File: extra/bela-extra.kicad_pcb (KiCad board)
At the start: 2 copper layers, 63 x 85.3 mm, 62 parts, among them P1 bbbp9, P10 GU128x64E-U100, P11 gu140x16j-7002, P12 digital_in, P13 digital_out, P14 ext_power, P2 bbbp8, P3 enc+btn1, P4 enc+btn2, P5 power_in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

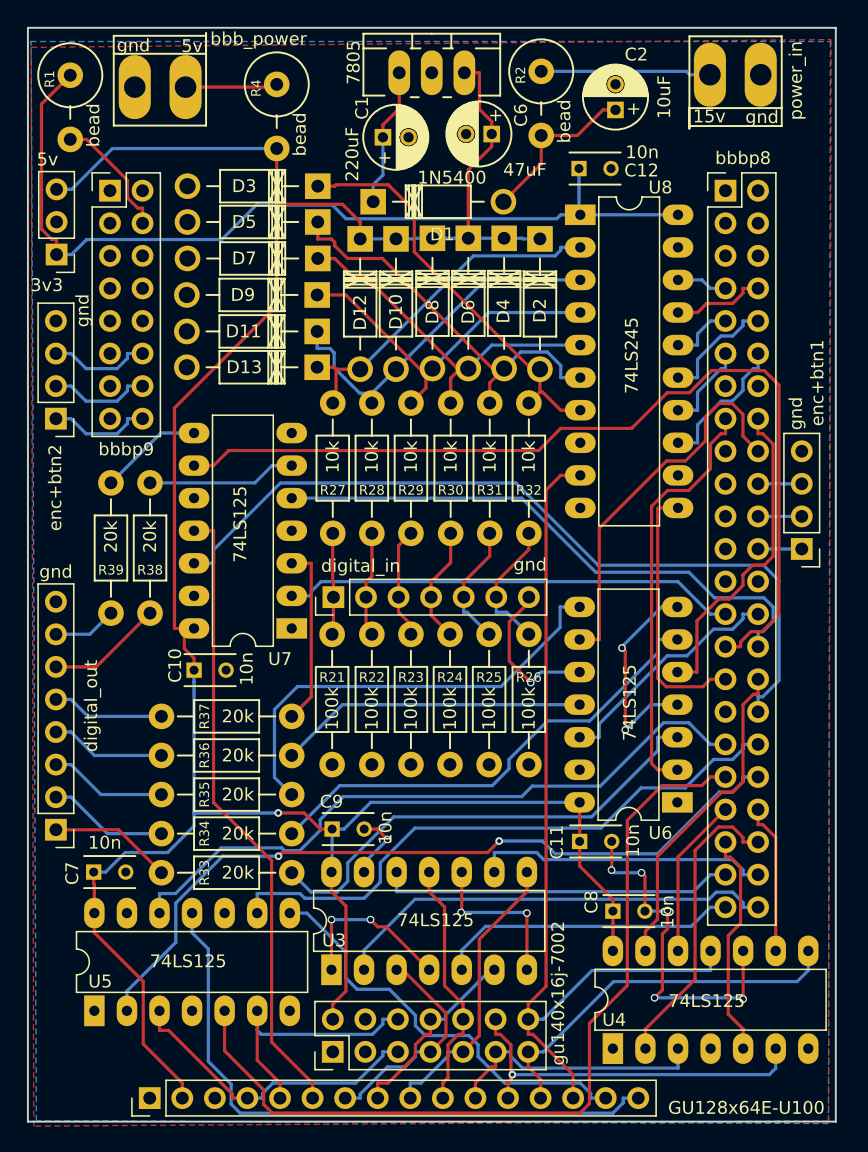
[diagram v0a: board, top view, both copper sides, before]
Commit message: ditched power, remapped a bunch of io
should have all the emmc and lcd lines disabled at boot
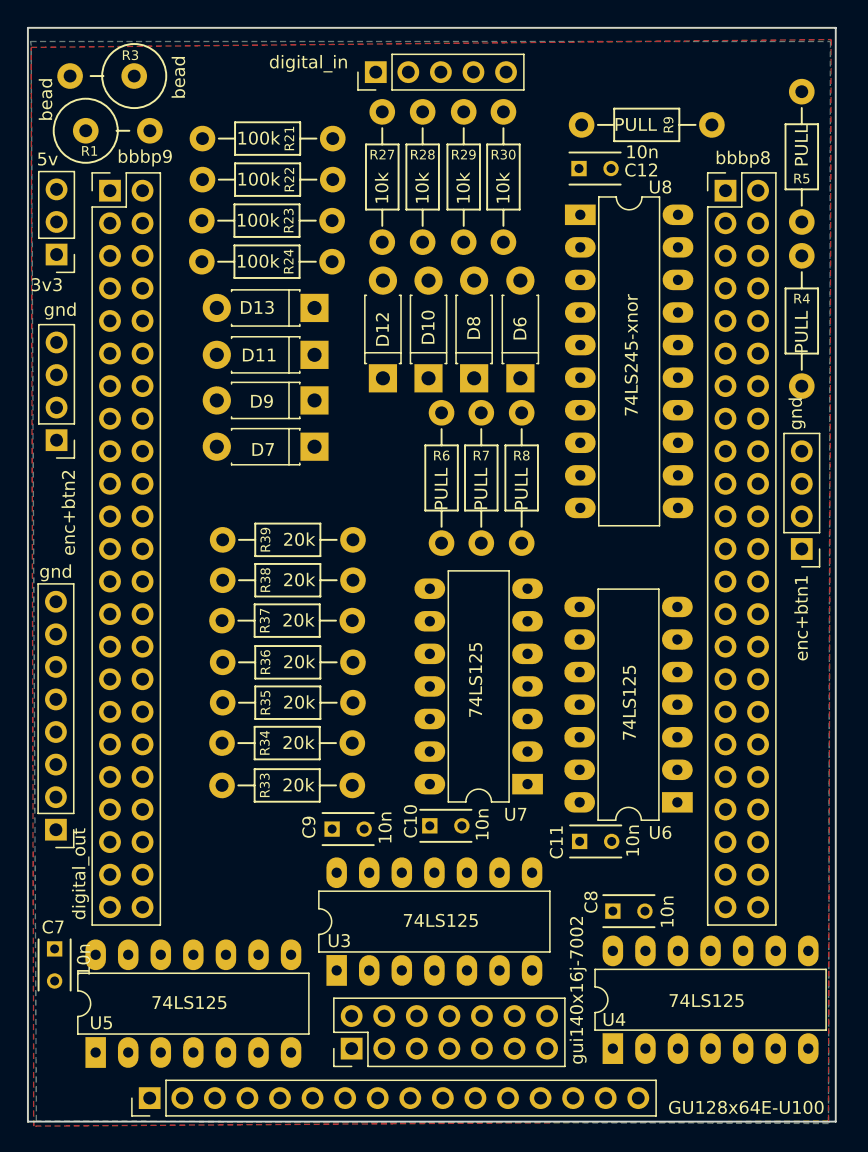
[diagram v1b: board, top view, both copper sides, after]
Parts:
- removed C1: 220uF, Capacitors_ThroughHole:C_Radial_D5_L11_P2
- removed C2: 10uF, Capacitors_ThroughHole:C_Radial_D5_L11_P2
- removed C6: 47uF, Capacitors_ThroughHole:C_Radial_D5_L11_P2
- removed D1: 1N5400, Diodes_ThroughHole:Diode_DO-41_SOD81_Horizontal_RM10
- removed D2, D3, D4, D5: D, Diodes_ThroughHole:Diode_DO-41_SOD81_Horizontal_RM10
- removed P5: power_in, mta-156:MTA-156-2
- removed P6: bbb_power, mta-156:MTA-156-2
- removed R2: bead, xnorman:Resistor_Vertical_RM5mm-xnor
- removed R25, R26: 100k, xnorman:Resistor_Horizontal_RM10mm-xnorman
- removed R31, R32: 10k, xnorman:Resistor_Horizontal_RM10mm-xnorman
- removed U2: 7805, TO_SOT_Packages_THT:TO-220_Neutral123_Vertical_LargePads
- added R3: bead, xnorman:Resistor_Vertical_RM5mm-xnor, F.Cu at (24.8, 16.5)
- added R5: PULL, xnorman:Resistor_Horizontal_RM10mm-xnorman, F.Cu at (79.3, 17.7)
- added R6: PULL, xnorman:Resistor_Horizontal_RM10mm-xnorman, F.Cu at (51.3, 52.9)
- added R7: PULL, xnorman:Resistor_Horizontal_RM10mm-xnorman, F.Cu at (54.4, 52.9)
- added R8: PULL, xnorman:Resistor_Horizontal_RM10mm-xnorman, F.Cu at (57.5, 52.9)
- added R9: PULL, xnorman:Resistor_Horizontal_RM10mm-xnorman, F.Cu at (62.2, 20.3)
- D10, D11, D12, D13, D6, D7, D8, D9: footprint Diodes_ThroughHole:Diode_DO-41_SOD81_Horizontal_RM10 -> Diodes_ThroughHole:D_DO-41_SOD81_P7.62mm_Horizontal
- P1: footprint Pin_Headers:Pin_Header_Straight_2x08_Pitch2.54mm -> Pin_Headers:Pin_Header_Straight_2x23_Pitch2.54mm
- P11: value gu140x16j-7002 -> gui140x16j-7002
- P12: footprint Pin_Headers:Pin_Header_Straight_1x07_Pitch2.54mm -> Pin_Headers:Pin_Header_Straight_1x05_Pitch2.54mm
- R4: value bead -> PULL; footprint xnorman:Resistor_Vertical_RM5mm-xnor -> xnorman:Resistor_Horizontal_RM10mm-xnorman
- U8: value 74LS245 -> 74LS245-xnor
- moved R21 49.9 mm to (32.6, 21.3), turned to 0 degrees
- moved R22 47.5 mm to (32.6, 24.5), turned to 0 degrees
- moved R4 46.0 mm to (79.3, 40.6), turned to 90 degrees
- moved R23 45.4 mm to (32.6, 27.7), turned to 0 degrees
- moved R24 43.7 mm to (32.6, 30.9), turned to 0 degrees
- moved P12 41.1 mm to (46.1, 16.2)
- moved C10 22.0 mm to (50.3, 74.9)
- moved U7 22.0 mm to (58.0, 71.7)
- moved R39 19.4 mm to (44.3, 52.6), turned to 180 degrees
- moved R38 17.6 mm to (44.3, 55.8), turned to 180 degrees
- moved D7 14.7 mm to (41.4, 45.4)
- moved R29 13.2 mm to (53.0, 29.4), turned to 90 degrees
- moved R30 13.2 mm to (56.1, 29.4), turned to 90 degrees
- moved R28 13.2 mm to (49.8, 29.4), turned to 90 degrees
- moved R27 13.1 mm to (46.6, 29.4), turned to 90 degrees
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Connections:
- P1 pad 1: (no net) -> GND
- P1 pad 2: (no net) -> GND
- P1 pad 5: (no net) -> Net-(P1-Pad5)
- P12 pad 5: Net-(P12-Pad5) -> GND
- P2 pad 11: beladigin5 -> bb-digitalInEnable
- P2 pad 12: beladigin6 -> bb-vfdCTRLenable
- P2 pad 13: (no net) -> bb-encin1-btn
- P2 pad 14: (no net) -> bb-vfdDOUTenable
- P2 pad 20: encin1-btn -> (no net)
- P2 pad 22: encin1-b -> (no net)
- P2 pad 24: encin1-a -> (no net)
- P2 pad 32: bb-vfdD7enable -> bb-encin1-b
- P2 pad 33: (no net) -> bb-encin1-a
- R4 pad 1: Net-(P6-Pad1) -> bb-vfdDOUTenable
- U3 pad 1: GND -> bb-vfdDOUTenable
- U3 pad 10: GND -> bb-vfdDOUTenable
- U3 pad 13: GND -> bb-vfdDOUTenable
- U3 pad 4: GND -> bb-vfdDOUTenable
- U4 pad 1: GND -> bb-vfdDOUTenable
- U4 pad 10: GND -> bb-vfdDOUTenable
- U4 pad 13: bb-vfdD7enable -> bb-vfdDOUTenable
- U4 pad 4: GND -> bb-vfdDOUTenable
- U5 pad 1: GND -> bb-vfdCTRLenable
- U5 pad 10: GND -> bb-vfdCTRLenable
- U5 pad 13: GND -> bb-vfdCTRLenable
- U5 pad 4: GND -> bb-vfdCTRLenable
- U7 pad 13: GND -> bb-vfdCTRLenable
- U8 pad 12: (no net) -> bb-encin1-btn
- U8 pad 13: beladigin6 -> bb-encin1-b
- U8 pad 14: beladigin5 -> bb-encin1-a
- U8 pad 19: GND -> bb-digitalInEnable
- U8 pad 6: moddigin5 -> encin1-a
- U8 pad 7: moddigin6 -> encin1-b
- U8 pad 8: GND -> encin1-btn
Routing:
- net 5v: track 203.8 -> 0.00 mm, vias 1 -> 0
- net GND: track 88.1 -> 0.00 mm, vias 13 -> 0
- net beladigout7: track 72.5 -> 0.00 mm
- net vfdD7: track 70.1 -> 0.00 mm
- net 3.3v: track 70.1 -> 0.00 mm
- net bb-vfd-RD+RW: track 66.9 -> 0.00 mm
- net bb-vfdE: track 63.1 -> 0.00 mm
- net bb-vfd-WR+RS: track 60.5 -> 0.00 mm, vias 2 -> 0
- net bb-vfdCS2: track 52.5 -> 0.00 mm
- net vfdE: track 49.0 -> 0.00 mm
- net vfdCS2: track 48.9 -> 0.00 mm
- net bb-vfdCS1: track 46.8 -> 0.00 mm
- net beladigout6: track 44.9 -> 0.00 mm
- net moddigout2: track 37.4 -> 0.00 mm
- net moddigout1: track 37.2 -> 0.00 mm
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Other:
- board text removed: "+"
- board text removed: "15v"

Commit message: connected up the rest of the extra board
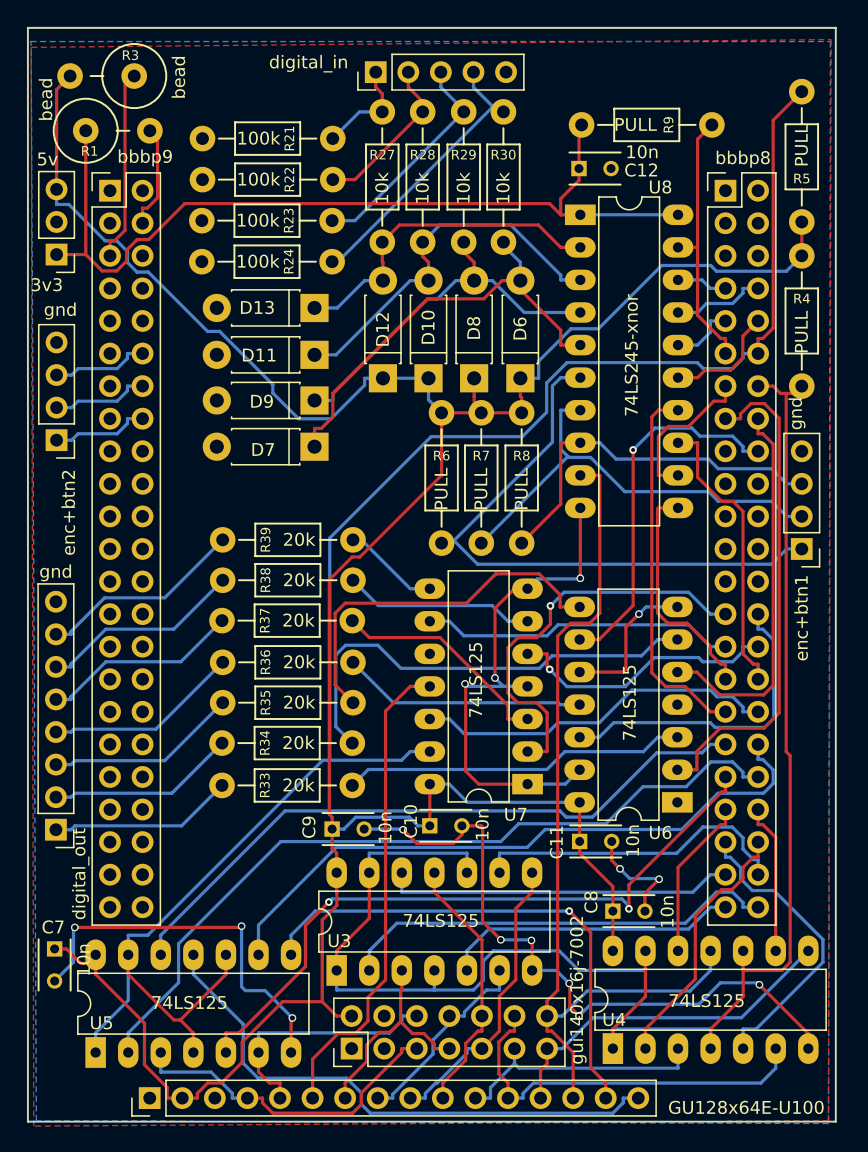
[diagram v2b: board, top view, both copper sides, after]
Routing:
- net 5v: track 0.00 -> 216.7 mm
- net GND: track 0.00 -> 146.6 mm, vias 0 -> 15
- net bb-vfdCTRLenable: track 0.00 -> 136.9 mm
- net bb-vfdDOUTenable: track 0.00 -> 131.0 mm
- net vfdD7: track 0.00 -> 69.5 mm
- net 3.3v: track 0.00 -> 69.4 mm
- net bb-vfd-WR+RS: track 0.00 -> 61.9 mm
- net bb-vfd-RD+RW: track 0.00 -> 53.2 mm, vias 0 -> 2
- net bb-vfdCS2: track 0.00 -> 52.1 mm
- net bb-vfdCS1: track 0.00 -> 50.8 mm
- net encin1-a: track 0.00 -> 47.1 mm
- net vfdCS2: track 0.00 -> 43.7 mm
- net vfdCS1: track 0.00 -> 39.8 mm, vias 0 -> 1
- net beladigout1: track 0.00 -> 38.9 mm
- net vfdE: track 0.00 -> 37.6 mm
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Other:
- board text added: "xnor 3/17"
- board text removed: "xnor 1/17"

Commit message: fixed up some labels
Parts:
- P13: value digital_out -> dig_out
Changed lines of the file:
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@@
       (effects (font (size 1 1) (thickness 0.15)))
     )
-    (fp_text value 10n (at 0.8636 -2.286 450) (layer F.SilkS)
+    (fp_text value 10n (at 4.3688 0 540) (layer F.SilkS)
       (effects (font (size 1 1) (thickness 0.15)))
     )
@@
     (descr "Film Capacitor Length 4mm x Width 2.5mm, Pitch 2.5mm")
     (tags Capacitor)
-    (fp_text reference C8 (at -1.6764 -0.7112 90) (layer F.SilkS)
+    (fp_text reference C8 (at -0.2032 -2.0828 180) (layer F.SilkS)
       (effects (font (size 1 1) (thickness 0.15)))
     )
@@
     (descr "Film Capacitor Length 4mm x Width 2.5mm, Pitch 2.5mm")
     (tags Capacitor)
-    (fp_text reference C10 (at -1.4732 -0.3556 90) (layer F.SilkS)
+    (fp_text reference C10 (at -1.6256 0.1524 90) (layer F.SilkS)
       (effects (font (size 1 1) (thickness 0.15)))
     )
@@
       (effects (font (size 1 1) (thickness 0.15)))
     )
-    (fp_text value digital_out (at -1.8288 -3.4544 270) (layer F.SilkS)
+    (fp_text value dig_out (at -1.5748 -4.4704 270) (layer F.SilkS)
       (effects (font (size 1 1) (thickness 0.15)))
     )
@@
     (descr "20-lead dip package, row spacing 7.62 mm (300 mils), LongPads")
     (tags "DIL DIP PDIP 2.54mm 7.62mm 300mil LongPads")
-    (fp_text reference U8 (at 6.2484 -2.1336) (layer F.SilkS)
+    (fp_text reference U8 (at 8.128 -2.4384) (layer F.SilkS)
       (effects (font (size 1 1) (thickness 0.15)))
     )
@@
     (descr "Film Capacitor Length 4mm x Width 2.5mm, Pitch 2.5mm")
     (tags Capacitor)
-    (fp_text reference C12 (at 4.8768 0.1524) (layer F.SilkS)
-      (effects (font (size 1 1) (thickness 0.15)))
-    )
-    (fp_text value 10n (at 4.9276 -1.27) (layer F.SilkS)
+    (fp_text reference C12 (at -1.778 -0.254 90) (layer F.SilkS)
+      (effects (font (size 1 1) (thickness 0.15)))
+    )
+    (fp_text value 10n (at 4.2164 -0.1016 90) (layer F.SilkS)
       (effects (font (size 1 1) (thickness 0.15)))
     )
@@
       (effects (font (size 1 1) (thickness 0.15)))
     )
-    (fp_text value digital_in (at 0.762 -5.2324 180) (layer F.SilkS)
+    (fp_text value digital_in (at 2.3876 1.9812 180) (layer F.SilkS)
       (effects (font (size 1 1) (thickness 0.15)))
     )
@@
     (effects (font (size 1 1) (thickness 0.15)))
   )
-  (gr_text 3v3 (at 20.4724 32.766) (layer F.SilkS)
+  (gr_text 3v3 (at 21.4376 32.7152) (layer F.SilkS)
     (effects (font (size 1 1) (thickness 0.15)))
   )
